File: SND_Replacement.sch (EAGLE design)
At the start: 35 parts, among them IC1 TL072P, IC2 4016N, IC3 74LS05N, IC4 555, Q1 2N3906, Q2 2N3904

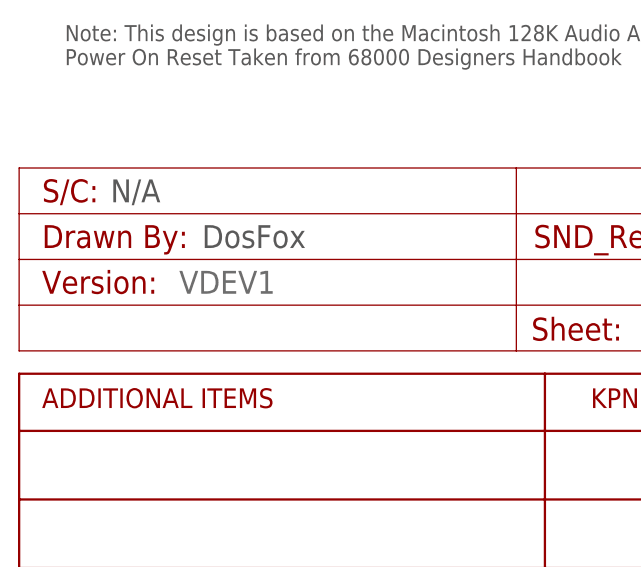
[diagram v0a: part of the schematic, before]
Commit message: Add files via upload
Resolved issue regarding R11 (200K rather than original 68K
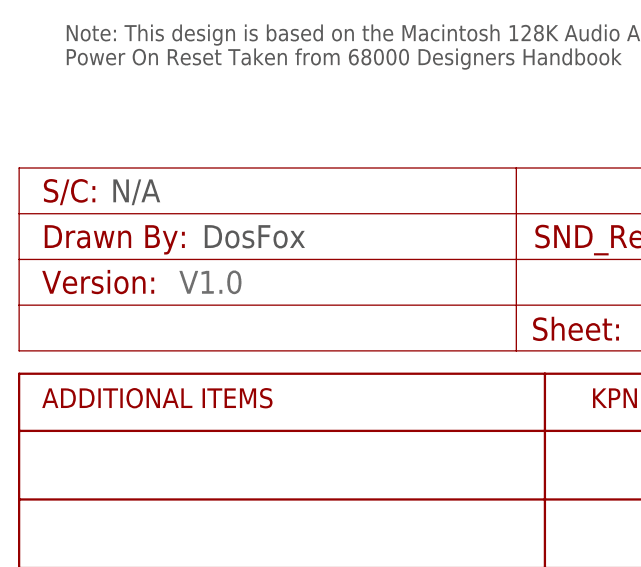
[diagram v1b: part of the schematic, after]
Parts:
- A1: value VDEV1 -> V1.0
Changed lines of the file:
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@@
 </classes>
 <parts>
-<part name="A1" library="Schematic Symbols" deviceset="PROJECT_DETAILS" device="_CUSTOM" value="VDEV1"/>
+<part name="A1" library="Schematic Symbols" deviceset="PROJECT_DETAILS" device="_CUSTOM" value="V1.0"/>
 <part name="IC1" library="linear" library_urn="urn:adsk.eagle:library:262" deviceset="TL072" device="P" package3d_urn="urn:adsk.eagle:package:16409/2"/>
 <part name="IC2" library="40xx" library_urn="urn:adsk.eagle:library:80" deviceset="4016" device="N" package3d_urn="urn:adsk.eagle:package:16407/2"/>
